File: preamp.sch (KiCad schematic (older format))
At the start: 2 parts

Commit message: no idea what to write.
something :-D
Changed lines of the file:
@@
 $Descr A4 11693 8268
 encoding utf-8
-Sheet 1 7
+Sheet 1 8
 Title ""
 Date ""
@@
 $EndDescr
 $Sheet
-S 2000 825  675  325
+S 3025 825  675  325
 U 5882A13F
 F0 "surge" 60
 F1 "surge.sch" 60
-F2 "L_I" I L 2000 900 60
-F3 "PE_I" O L 2000 975 60
-F4 "N_I" O L 2000 1050 60
-F5 "L_O" O R 2675 900 60
-F6 "PE_O" I R 2675 975 60
-F7 "N_O" I R 2675 1050 60
+F2 "L_I" I L 3025 900 60
+F3 "PE_I" O L 3025 975 60
+F4 "N_I" O L 3025 1050 60
+F5 "L_O" O R 3700 900 60
+F6 "PE_O" I R 3700 975 60
+F7 "N_O" I R 3700 1050 60
 $EndSheet
 $Comp
@@
 $EndComp
 $Sheet
-S 2975 825  775  325
+S 4000 825  775  325
 U 58836B99
 F0 "polarity_protection" 60
 F1 "polarity_protection.sch" 60
-F2 "L_I" I L 2975 900 60
-F3 "PE_I" O L 2975 975 60
-F4 "N_I" O L 2975 1050 60
-F5 "L_O" O R 3750 900 60
-F6 "PE_O" I R 3750 975 60
-F7 "N_O" I R 3750 1050 60
-$EndSheet
-Wire Wire Line
-	2675 900  2975 900
-Wire Wire Line
-	2975 975  2675 975
-Wire Wire Line
-	2675 1050 2975 1050
-$Sheet
-S 4750 825  925  725
+F2 "L_I" I L 4000 900 60
+F3 "PE_I" O L 4000 975 60
+F4 "N_I" O L 4000 1050 60
+F5 "L_O" O R 4775 900 60
+F6 "PE_O" I R 4775 975 60
+F7 "N_O" I R 4775 1050 60
+$EndSheet
+Wire Wire Line
+	3700 900  4000 900
+Wire Wire Line
+	4000 975  3700 975
+Wire Wire Line
+	3700 1050 4000 1050
+$Sheet
+S 5450 825  925  725
 U 58838AD0
 F0 "relaisboard" 60
 F1 "relaisboard.sch" 60
-F2 "L_I" I L 4750 900 60
-F3 "PE_I" O L 4750 975 60
-F4 "N_I" O L 4750 1050 60
-F5 "PE_O" I R 5675 975 60
-F6 "N_O" I R 5675 1050 60
-F7 "L1" O R 5675 1150 60
-F8 "L2" O R 5675 1225 60
-F9 "L3" O R 5675 1300 60
-F10 "L4" O R 5675 1375 60
-F11 "L5" O R 5675 1450 60
-F12 "GND" O L 4750 1250 60
-F13 "VCC" I L 4750 1175 60
-F14 "SCL" I L 4750 1350 60
-F15 "SDA" B L 4750 1425 60
-$EndSheet
-Wire Wire Line
-	4750 900  3750 900
-Wire Wire Line
-	3750 975  4750 975
-Wire Wire Line
-	4750 1050 3750 1050
-$Sheet
-S 2000 1625 1325 925
+F2 "L_I" I L 5450 900 60
+F3 "PE_I" O L 5450 975 60
+F4 "N_I" O L 5450 1050 60
+F5 "PE_O" I R 6375 975 60
+F6 "N_O" I R 6375 1050 60
+F7 "L1" O R 6375 1150 60
+F8 "L2" O R 6375 1225 60
+F9 "L3" O R 6375 1300 60
+F10 "L4" O R 6375 1375 60
+F11 "L5" O R 6375 1450 60
+F12 "GND" O L 5450 1250 60
+F13 "VCC" I L 5450 1175 60
+F14 "SCL" I L 5450 1350 60
+F15 "SDA" B L 5450 1425 60
+$EndSheet
+Wire Wire Line
+	5450 900  4775 900
+Wire Wire Line
+	4775 975  5450 975
+Wire Wire Line
+	5450 1050 4775 1050
+$Sheet
+S 2000 3125 1325 925
 U 5883E969
 F0 "case" 60
 F1 "case.sch" 60
-F2 "GND_preamp" I L 2000 1775 60
-F3 "PE_I" O L 2000 1700 60
-F4 "GND" O L 2000 1975 60
-F5 "VCC" O L 2000 1900 60
-F6 "Toslink_RX1" O R 3325 1675 60
-F7 "Toslink_RX2" O R 3325 1750 60
-F8 "Toslink_RX3" O R 3325 1825 60
-F9 "Toslink_RX4" O R 3325 1900 60
-F10 "Toslink_RX5" O R 3325 1975 60
-F11 "Toslink_RX6" O R 3325 2050 60
-F12 "Toslink_TX1" O R 3325 2175 60
-$EndSheet
-$Sheet
-S 1975 4500 1575 1425
+F2 "GND_preamp" I L 2000 3275 60
+F3 "PE_I" O L 2000 3200 60
+F4 "GND" O L 2000 3475 60
+F5 "VCC" O L 2000 3400 60
+F6 "Toslink_RX1" O R 3325 3175 60
+F7 "Toslink_RX2" O R 3325 3250 60
+F8 "Toslink_RX3" O R 3325 3325 60
+F9 "Toslink_RX4" O R 3325 3400 60
+F10 "Toslink_RX5" O R 3325 3475 60
+F11 "Toslink_RX6" O R 3325 3550 60
+F12 "Toslink_TX1" O R 3325 3675 60
+$EndSheet
+$Sheet
+S 1975 6000 1575 1425
 U 58843538
 F0 "odroid" 60
 F1 "odroid.sch" 60
-F2 "SCL" O R 3550 4550 60
-F3 "SDA" B R 3550 4625 60
-$EndSheet
-$Sheet
-S 1975 2825 1575 1400
+F2 "SCL" O R 3550 6050 60
+F3 "SDA" B R 3550 6125 60
+$EndSheet
+$Sheet
+S 1975 4325 1575 1400
 U 5885CB61
 F0 "spdif_i2s" 60
 F1 "spdif_i2s.sch" 60
-F2 "RESET" I L 1975 3750 60
-F3 "SDOUT" O L 1975 2975 60
-F4 "SDIN" I L 1975 2900 60
-F5 "SCLK" I L 1975 3050 60
-F6 "CSB" I L 1975 3125 60
-F7 "GPO1" O L 1975 3350 60
-F8 "GPO0" O L 1975 3275 60
-F9 "Toslink_TX0" O R 3550 2900 60
-F10 "Toslink_RX7" I R 3550 3575 60
-F11 "Toslink_RX6" I R 3550 3500 60
-F12 "Toslink_RX5" I R 3550 3425 60
-F13 "Toslink_RX4" I R 3550 3350 60
-F14 "Toslink_RX3" I R 3550 3275 60
-F15 "Toslink_RX2" I R 3550 3200 60
-F16 "Toslink_RX1" I R 3550 3125 60
-F17 "Toslink_RX0" I R 3550 3050 60
-F18 "MasterClock" B L 1975 3850 60
-F19 "BitClock" B L 1975 3925 60
-F20 "LRClock" B L 1975 4000 60
-F21 "DOUT" O L 1975 4075 60
-F22 "DIN" I L 1975 4150 60
-F23 "DVDD" I L 1975 3500 60
-F24 "AVDD" I L 1975 3575 60
-F25 "GND" I L 1975 3650 60
+F2 "RESET" I L 1975 5250 60
+F3 "SDOUT" O L 1975 4475 60
+F4 "SDIN" I L 1975 4400 60
+F5 "SCLK" I L 1975 4550 60
+F6 "CSB" I L 1975 4625 60
+F7 "GPO1" O L 1975 4850 60
+F8 "GPO0" O L 1975 4775 60
+F9 "Toslink_TX0" O R 3550 4400 60
+F10 "Toslink_RX7" I R 3550 5075 60
+F11 "Toslink_RX6" I R 3550 5000 60
+F12 "Toslink_RX5" I R 3550 4925 60
+F13 "Toslink_RX4" I R 3550 4850 60
+F14 "Toslink_RX3" I R 3550 4775 60
+F15 "Toslink_RX2" I R 3550 4700 60
+F16 "Toslink_RX1" I R 3550 4625 60
+F17 "Toslink_RX0" I R 3550 4550 60
+F18 "MasterClock" B L 1975 5350 60
+F19 "BitClock" B L 1975 5425 60
+F20 "LRClock" B L 1975 5500 60
+F21 "DOUT" O L 1975 5575 60
+F22 "DIN" I L 1975 5650 60
+F23 "DVDD" I L 1975 5000 60
+F24 "AVDD" I L 1975 5075 60
+F25 "GND" I L 1975 5150 60
 $EndSheet
 $Comp
@@
 	1325 900  1125 900
 Wire Wire Line
-	1175 975  1275 975
-Wire Wire Line
-	1275 975  1325 975
+	1175 975  1325 975
 Wire Wire Line
 	1175 1050 1325 1050
 Wire Wire Line
-	1800 900  2000 900
-Wire Wire Line
-	1800 975  2000 975
-Wire Wire Line
-	1800 1050 2000 1050
-Wire Wire Line
-	2000 1700 1275 1700
-Wire Wire Line
-	1275 1700 1275 975
+	1800 900  3025 900
+Wire Wire Line
+	1800 975  3025 975
+Wire Wire Line
+	1800 1050 3025 1050
+Wire Wire Line
+	2000 3200 1275 3200
+Wire Wire Line
+	1275 3200 1275 975
 Connection ~ 1275 975
 Wire Wire Line
-	3325 2175 3625 2175
-Wire Wire Line
-	3625 2175 3625 2900
-Wire Wire Line
-	3625 2900 3550 2900
-Wire Wire Line
-	3550 3050 3800 3050
-Wire Wire Line
-	3800 3050 3800 1675
-Wire Wire Line
-	3800 1675 3325 1675
-Wire Wire Line
-	3550 3125 3875 3125
-Wire Wire Line
-	3875 3125 3875 1750
-Wire Wire Line
-	3875 1750 3325 1750
-Wire Wire Line
-	3325 1825 3950 1825
-Wire Wire Line
-	3950 1825 3950 3200
-Wire Wire Line
-	3950 3200 3550 3200
-Wire Wire Line
-	3550 3275 4025 3275
-Wire Wire Line
-	4025 3275 4025 1900
-Wire Wire Line
-	4025 1900 3325 1900
-Wire Wire Line
-	3325 1975 4100 1975
-Wire Wire Line
-	4100 1975 4100 3350
-Wire Wire Line
-	4100 3350 3550 3350
-Wire Wire Line
-	3550 3425 4175 3425
-Wire Wire Line
-	4175 3425 4175 2050
-Wire Wire Line
-	4175 2050 3325 2050
-Wire Wire Line
-	3550 4550 4425 4550
-Wire Wire Line
-	4425 4550 4425 1350
-Wire Wire Line
-	4425 1350 4750 1350
-Wire Wire Line
-	3550 4625 4500 4625
-Wire Wire Line
-	4500 4625 4500 1425
-Wire Wire Line
-	4500 1425 4750 1425
+	3325 3675 3625 3675
+Wire Wire Line
+	3625 3675 3625 4400
+Wire Wire Line
+	3625 4400 3550 4400
+Wire Wire Line
+	3550 4550 3800 4550
+Wire Wire Line
+	3800 4550 3800 3175
+Wire Wire Line
+	3800 3175 3325 3175
+Wire Wire Line
+	3550 4625 3875 4625
+Wire Wire Line
+	3875 4625 3875 3250
+Wire Wire Line
+	3875 3250 3325 3250
+Wire Wire Line
+	3325 3325 3950 3325
+Wire Wire Line
+	3950 3325 3950 4700
+Wire Wire Line
+	3950 4700 3550 4700
+Wire Wire Line
+	3550 4775 4025 4775
+Wire Wire Line
+	4025 4775 4025 3400
+Wire Wire Line
+	4025 3400 3325 3400
+Wire Wire Line
+	3325 3475 4100 3475
+Wire Wire Line
+	4100 3475 4100 4850
+Wire Wire Line
+	4100 4850 3550 4850
+Wire Wire Line
+	3550 4925 4175 4925
+Wire Wire Line
+	4175 4925 4175 3550
+Wire Wire Line
+	4175 3550 3325 3550
+Wire Wire Line
+	3550 6050 5075 6050
+Wire Wire Line
+	5075 6050 5075 1350
+Wire Wire Line
+	5075 1350 5450 1350
+Wire Wire Line
+	3550 6125 5150 6125
+Wire Wire Line
+	5150 6125 5150 1425
+Wire Wire Line
+	5150 1425 5450 1425
+$Sheet
+S 2000 1400 1325 725
+U 58A1535E
+F0 "digital_supply" 60
+F1 "digital_supply.sch" 60
+$EndSheet
 $EndSCHEMATC

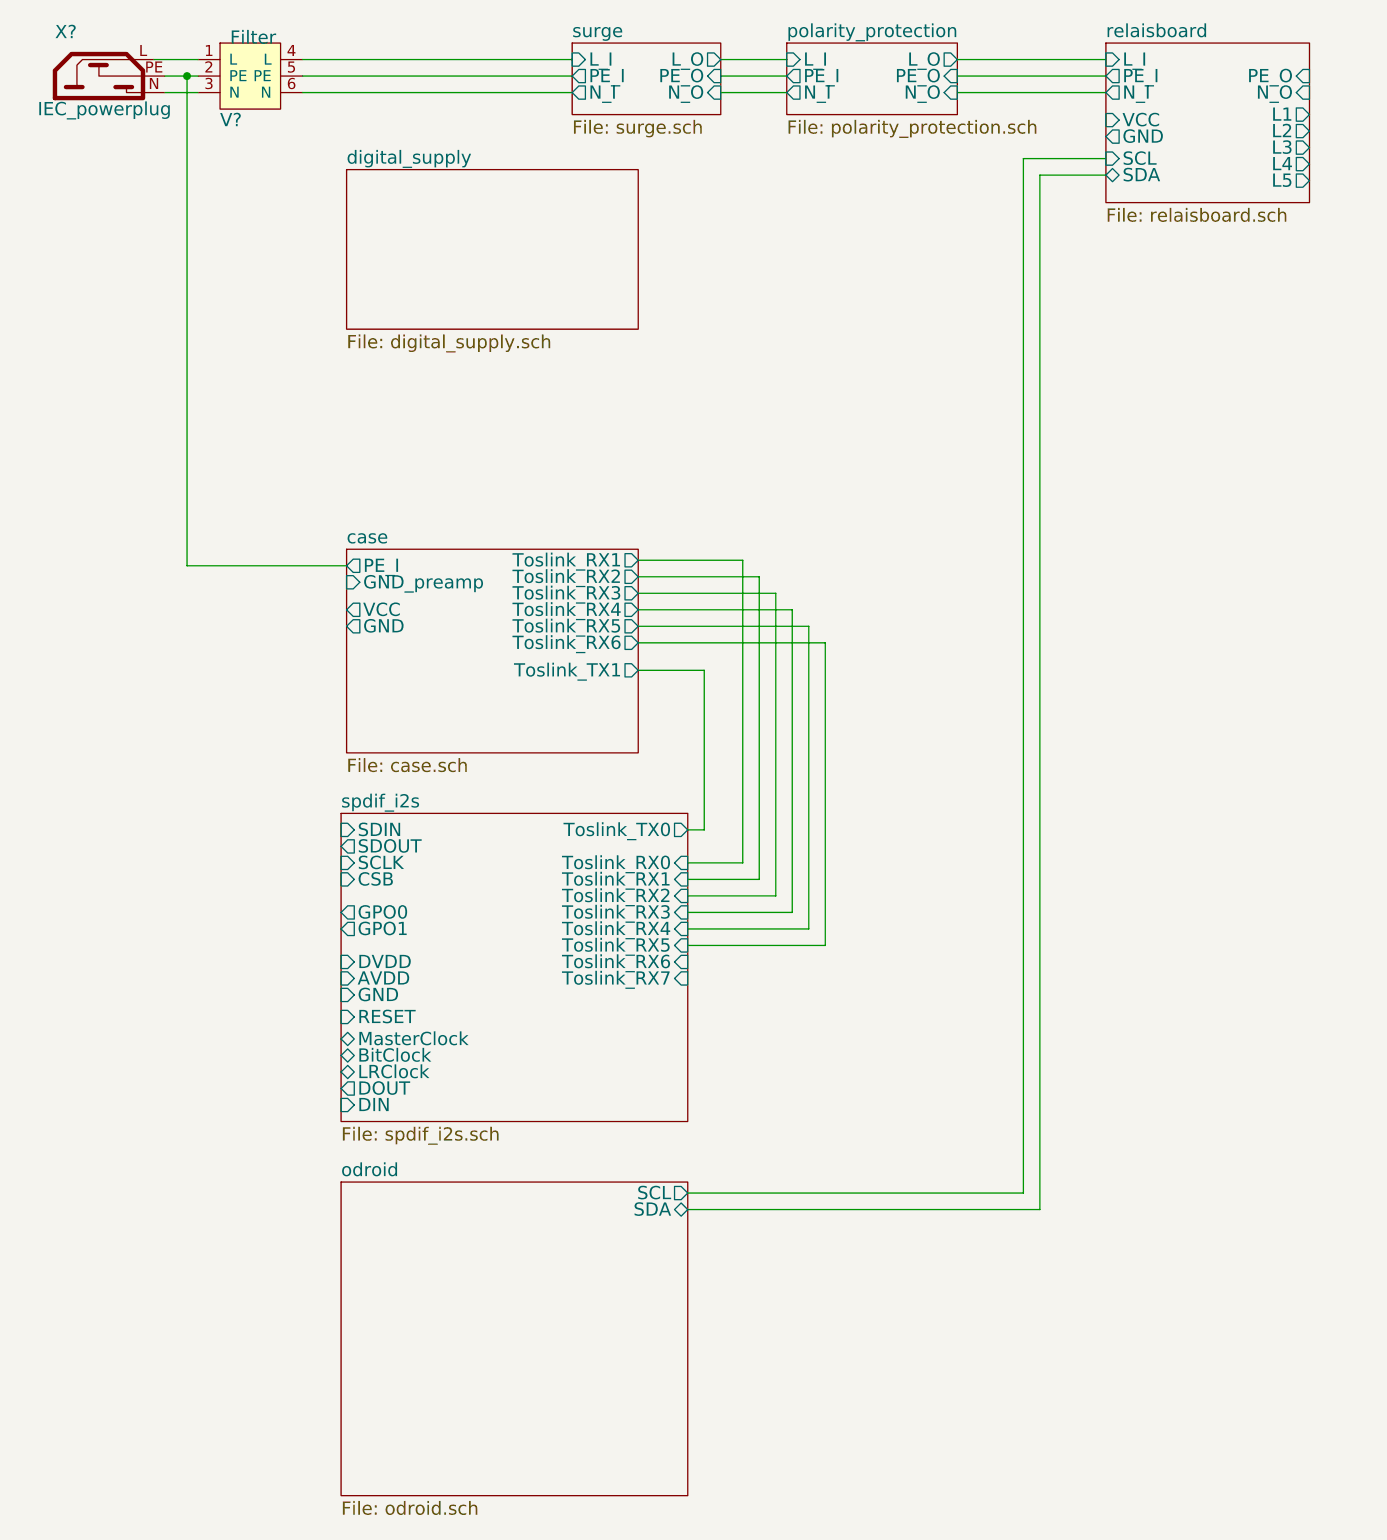
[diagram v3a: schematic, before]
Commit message: added teensy library
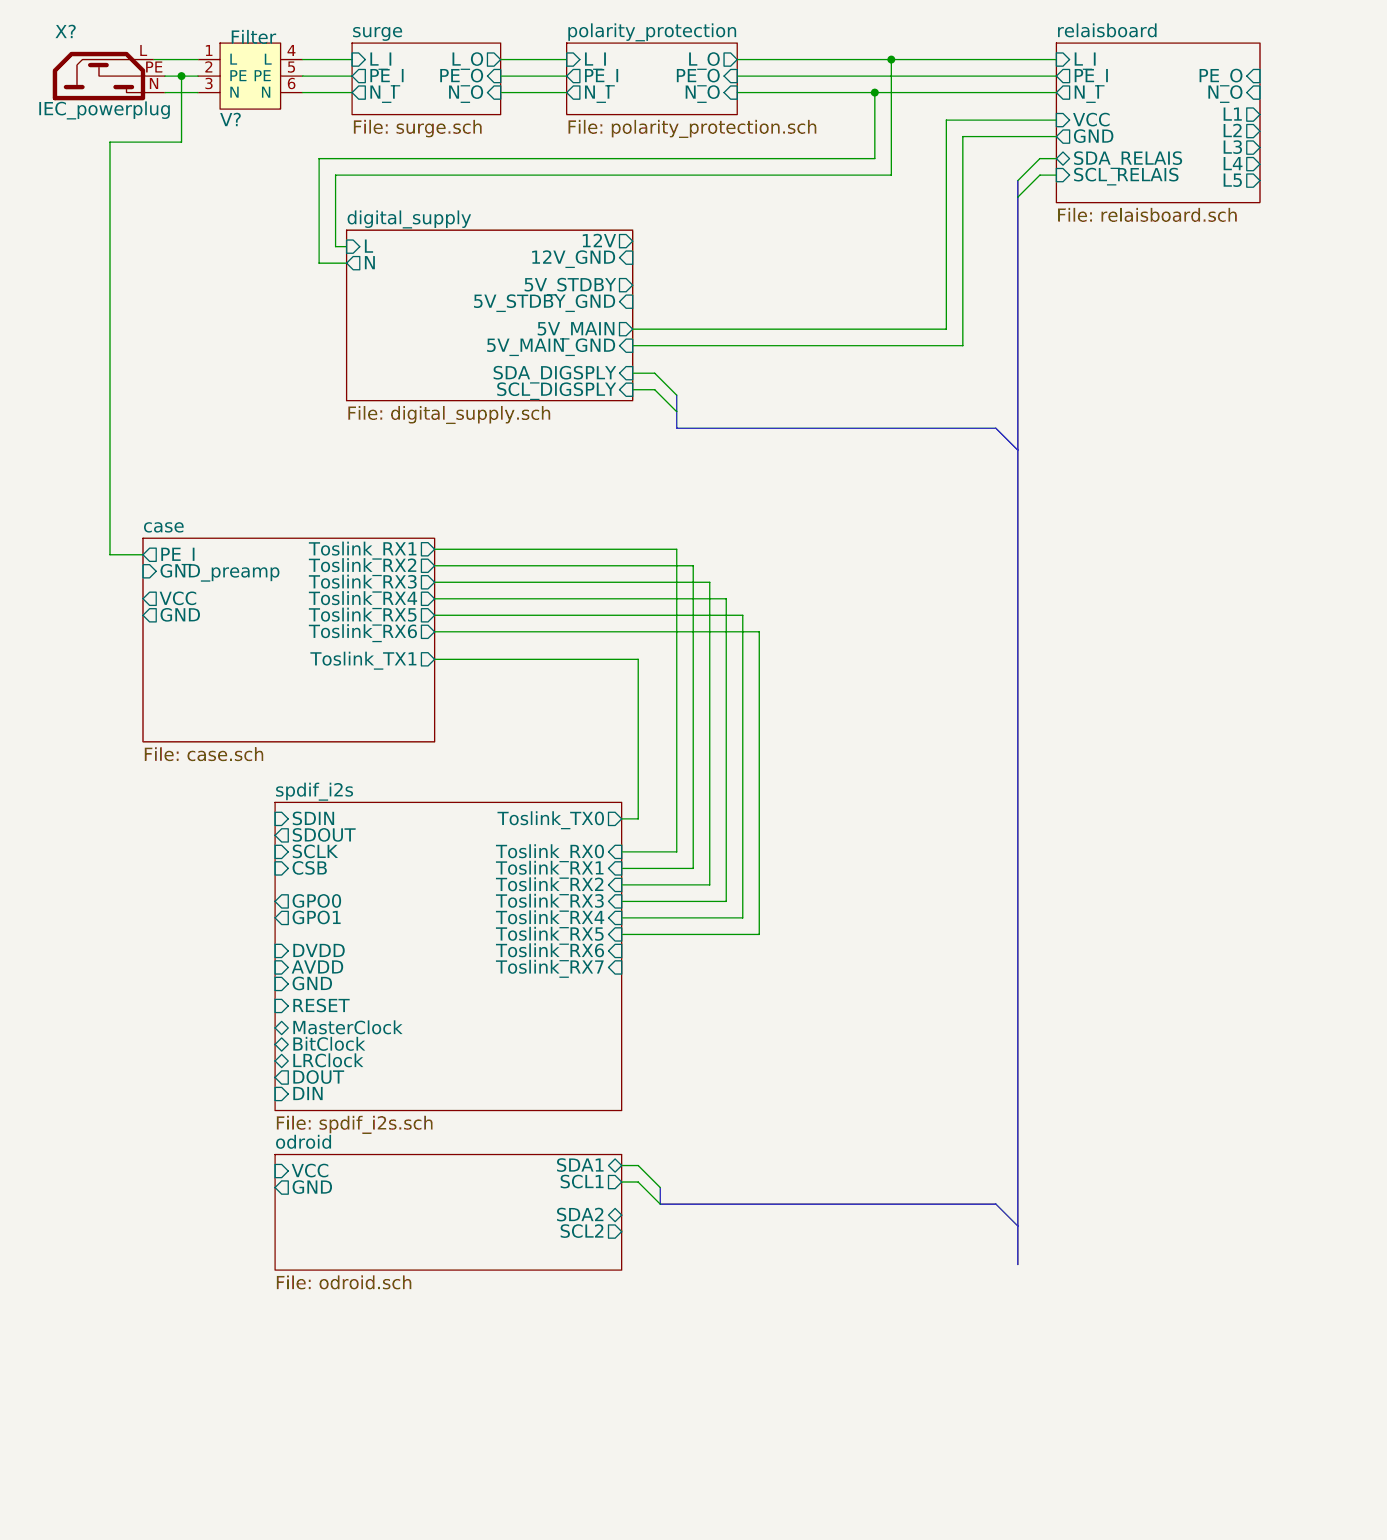
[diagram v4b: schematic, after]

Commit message: Weiterentwicklung des Netzteiles
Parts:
- removed V?: Filter, symbol Filter
- removed X?: IEC_powerplug, symbol IEC_power

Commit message: daily commit
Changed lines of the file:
@@
 	1375 2850 1375 3475
 Wire Bus Line
-	3500 4400 3500 4775
+	3500 4250 3500 4925
 Wire Wire Line
 	3250 4500 3400 4500
@@
 F15 "5V_MAIN" O R 2950 2375 60
 $EndSheet
+Entry Wire Line
+	3400 4950 3500 4850
+Entry Wire Line
+	3400 5025 3500 4925
+Wire Wire Line
+	3250 4950 3400 4950
+Wire Wire Line
+	3250 5025 3400 5025
+Entry Wire Line
+	3400 4350 3500 4250
+Wire Wire Line
+	3400 4350 3250 4350
 $EndSCHEMATC
